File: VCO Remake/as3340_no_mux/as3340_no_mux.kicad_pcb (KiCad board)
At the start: 2 copper layers, 20.3 x 118.1 mm, 68 parts, among them J1 Sync INput, J11 Conn_02x05_Odd_Even, J12 TRI OUt, J13 SIN OUT, J14 SAW OUt, J15 SQR OUT, J2 CV1, J4 LinearFmINput, J5 PWM INput, SW1 SW_SPDT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

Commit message: fp
front panel
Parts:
- added G***: LOGO, LOGO, F.Cu at (237.1, 100.6)
- added G***: LOGO, LOGO, F.Cu at (221.6, 27.9)
- added G***: LOGO, LOGO, F.Cu at (219.7, 151.1)
- added G***: LOGO, LOGO, F.Cu at (213.4, 36.7)
- added G***: LOGO, LOGO, F.Cu at (213.4, 51.3)
- added G***: LOGO, LOGO, F.Cu at (215.3, 27.9)
- added G***: LOGO, LOGO, F.Cu at (213.5, 65.9)
- added J1: Sync INput, AudioJacks:Jack_3.5mm_QingPu_WQP-PJ398SM_Vertical, F.Cu at (208.3, 119.4)
- added J12: TRI OUt, AudioJacks:Jack_3.5mm_QingPu_WQP-PJ398SM_Vertical, F.Cu at (218.4, 88.9)
- added J13: SIN OUT, AudioJacks:Jack_3.5mm_QingPu_WQP-PJ398SM_Vertical, F.Cu at (218.4, 104.1)
- added J14: SAW OUt, AudioJacks:Jack_3.5mm_QingPu_WQP-PJ398SM_Vertical, F.Cu at (218.4, 119.4)
- added J15: SQR OUT, AudioJacks:Jack_3.5mm_QingPu_WQP-PJ398SM_Vertical, F.Cu at (218.4, 134.6)
- added J2: CV1, AudioJacks:Jack_3.5mm_QingPu_WQP-PJ398SM_Vertical, F.Cu at (208.3, 88.9)
- added J4: LinearFmINput, AudioJacks:Jack_3.5mm_QingPu_WQP-PJ398SM_Vertical, F.Cu at (208.3, 104.1)
- added J5: PWM INput, AudioJacks:Jack_3.5mm_QingPu_WQP-PJ398SM_Vertical, F.Cu at (208.3, 134.6)
- added THONKY_COURSE_CV1: 100k Pot, Potentiometer_THT:Potentiometer_Alps_RK09K_Single_Vertical, F.Cu at (210.9, 44.1)
- added THONKY_FINE_CV1: 100k Pot, Potentiometer_THT:Potentiometer_Alps_RK09K_Single_Vertical, F.Cu at (210.9, 58.8)
- added THONKY_PWM1: 100k Pot, Potentiometer_THT:Potentiometer_Alps_RK09K_Single_Vertical, F.Cu at (210.9, 73.4)
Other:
- board size 20.3 x 118.1 mm -> 45.7 x 128.5 mm
- board text added: "Certain Synths VCO"
- board text added: "Course Tune"
- board text added: "Fine Tune"
- board text added: "Pulse Width"

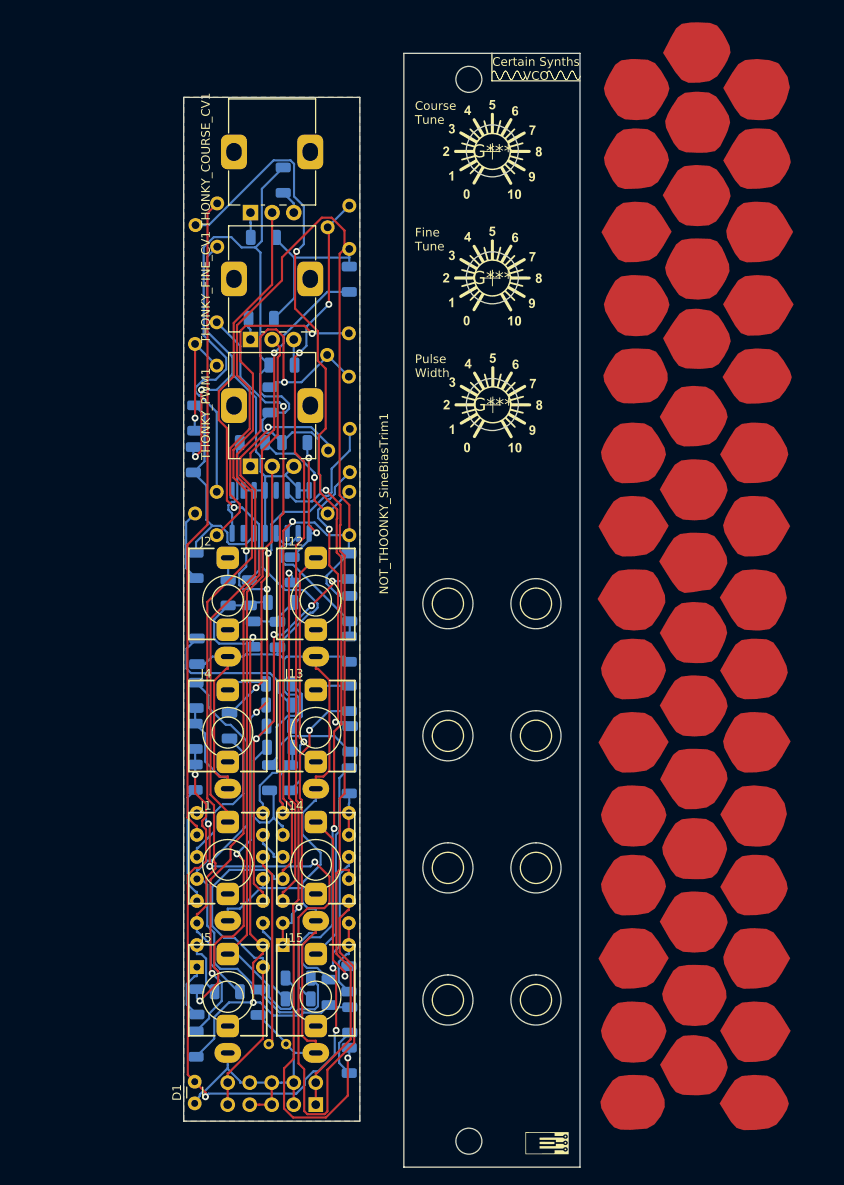
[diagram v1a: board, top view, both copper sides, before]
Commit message: Redone VCO Layout
Added the switch and made trace width .2mm
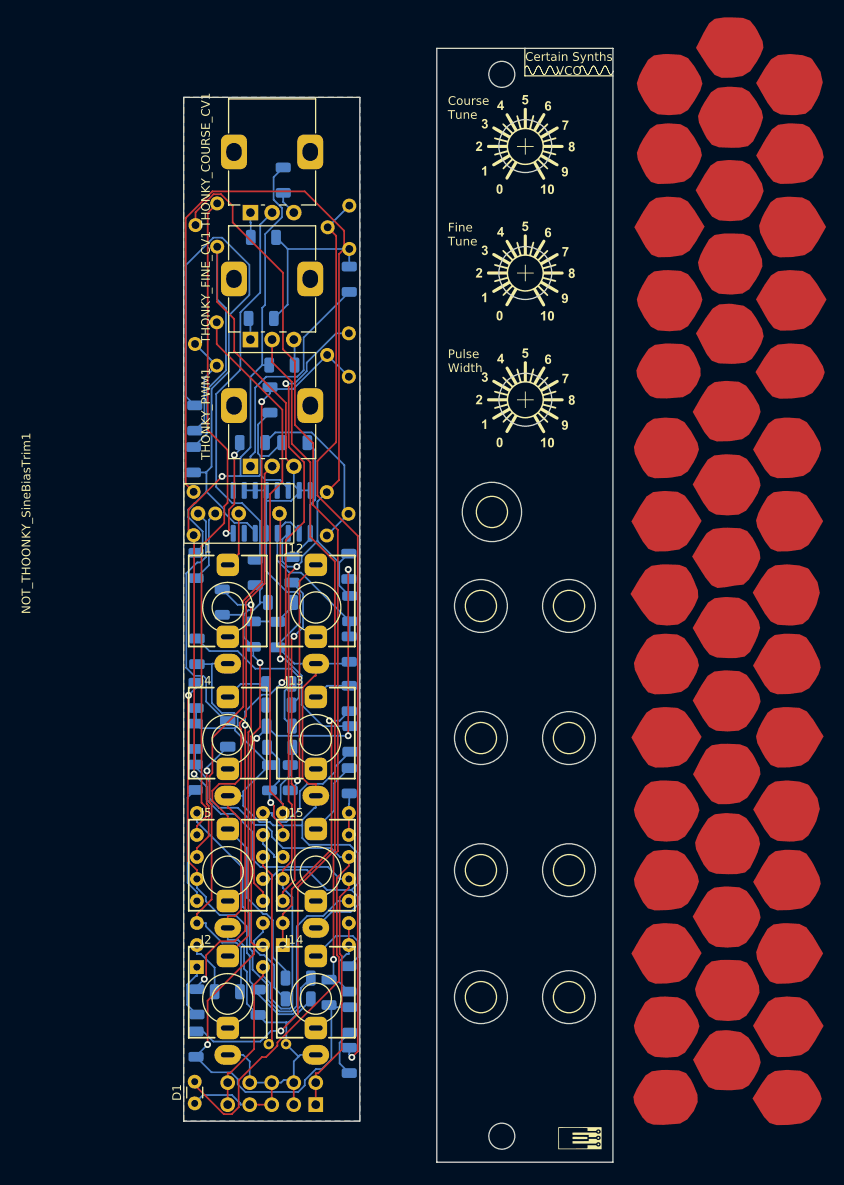
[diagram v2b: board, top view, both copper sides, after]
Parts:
- removed the G*** at (237.1, 100.6)
- removed the G*** at (221.6, 27.9)
- removed the G*** at (219.7, 151.1)
- removed the G*** at (213.4, 36.7)
- removed the G*** at (213.4, 51.3)
- removed the G*** at (215.3, 27.9)
- removed the G*** at (213.5, 65.9)
- removed the J1 at (208.3, 119.4)
- removed the J12 at (218.4, 88.9)
- removed the J13 at (218.4, 104.1)
- removed the J14 at (218.4, 119.4)
- removed the J15 at (218.4, 134.6)
- removed the J2 at (208.3, 88.9)
- removed the J4 at (208.3, 104.1)
- removed the J5 at (208.3, 134.6)
- added G***: LOGO, LOGO, F.Cu at (219.1, 27.4)
- added G***: LOGO, LOGO, F.Cu at (225.4, 27.4)
- added G***: LOGO, LOGO, F.Cu at (223.5, 150.6)
- added G***: LOGO, LOGO, F.Cu at (217.2, 36.1)
- added G***: LOGO, LOGO, F.Cu at (217.2, 65.4)
- added G***: LOGO, LOGO, F.Cu at (217.2, 50.7)
- added G***: LOGO, LOGO, F.Cu at (240.9, 100.0)
- added SLOTMAN: CV1, AudioJacks:Jack_3.5mm_QingPu_WQP-PJ398SM_Vertical, F.Cu at (213.4, 78.3)
- added Slot1: CV1, AudioJacks:Jack_3.5mm_QingPu_WQP-PJ398SM_Vertical, F.Cu at (212.1, 104.4)
- added Slot10: CV1, AudioJacks:Jack_3.5mm_QingPu_WQP-PJ398SM_Vertical, F.Cu at (222.2, 134.3)
- added Slot2: CV1, AudioJacks:Jack_3.5mm_QingPu_WQP-PJ398SM_Vertical, F.Cu at (222.2, 104.4)
- added Slot3: CV1, AudioJacks:Jack_3.5mm_QingPu_WQP-PJ398SM_Vertical, F.Cu at (212.1, 119.6)
- added Slot33: CV1, AudioJacks:Jack_3.5mm_QingPu_WQP-PJ398SM_Vertical, F.Cu at (212.1, 89.2)
- added Slot4: CV1, AudioJacks:Jack_3.5mm_QingPu_WQP-PJ398SM_Vertical, F.Cu at (222.2, 119.6)
- added Slot87: CV1, AudioJacks:Jack_3.5mm_QingPu_WQP-PJ398SM_Vertical, F.Cu at (222.2, 89.2)
- added Slot9: CV1, AudioJacks:Jack_3.5mm_QingPu_WQP-PJ398SM_Vertical, F.Cu at (212.1, 134.3)
- SW1: footprint Potentiometer_THT:Potentiometer_ACP_CA6-H2,5_Horizontal -> AAA MY Parts:Dailywell mini DWB1 SPDT; moved to F.Cu
- moved J2 45.9 mm to (182.9, 134.5)
- moved J1 29.7 mm to (182.9, 89.3)
- moved SW1 20.1 mm to (179.4, 78.5), turned to 0 degrees
- moved J14 15.5 mm to (193.0, 134.5)
- moved J15 14.4 mm to (193.0, 119.8)
- moved J5 14.4 mm to (182.9, 119.8)
- moved NOT_THINK_SineLevelTrim1 5.67 mm to (194.3, 81.0), turned to 0 degrees
- moved NOT_THOONKY_SineBiasTrim1 5.67 mm to (178.9, 81.0), turned to 0 degrees
- moved THONKY_COURSE_CV1 3.85 mm to (214.7, 43.6)
- moved THONKY_FINE_CV1 3.85 mm to (214.7, 58.2)
- moved THONKY_PWM1 3.85 mm to (214.7, 72.9)
- moved R20 2.45 mm to (186.1, 85.3)
- moved R24 1.28 mm to (182.2, 88.7)
- moved C7 0.96 mm to (182.9, 103.9)
- moved J12 0.81 mm to (193.0, 89.3)
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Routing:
- net Net-(SW1-B): track 59.0 -> 6.45 mm, vias 1 -> 0
- net Net-(U1A-+): track 26.7 -> 73.2 mm
- net Net-(J2-PadR): track 2.59 -> 45.7 mm, vias 0 -> 1
- net Net-(U2-VSO): track 81.7 -> 45.5 mm, vias 3 -> 0
- net -15V: track 173.7 -> 148.7 mm, vias 1 -> 2
- net Net-(NOT+THINKY_CV1-Pad1): track 123.0 -> 104.0 mm, vias 3 -> 1
- net Net-(D1-A): track 84.2 -> 67.4 mm, vias 4 -> 0
- net Net-(NOT_THONKY_HF_TRACK1-Pad2): track 117.1 -> 101.9 mm, vias 2 -> 1
- net Net-(NOT_THINKY_TEMKO1-Pad1): track 102.3 -> 87.6 mm, vias 6 -> 4
- net Net-(U2-VEE): track 103.5 -> 89.0 mm
- net Net-(J15-PadR): track 23.1 -> 8.63 mm
- net Net-(SW1-A): track 40.5 -> 28.2 mm, vias 2 -> 0
- net Net-(J14-PadR): track 20.5 -> 9.38 mm, vias 1 -> 0
- net Net-(R19-Pad1): track 85.3 -> 96.1 mm
- net Net-(U2-VFCI): track 81.7 -> 92.4 mm
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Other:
- board size 45.7 x 128.5 mm -> 49.5 x 128.5 mm
- board text added: "100k"
- board text added: "20k"
- board text added: "470k"
